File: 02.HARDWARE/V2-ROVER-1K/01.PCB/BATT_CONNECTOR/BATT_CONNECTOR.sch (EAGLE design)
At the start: 16 parts, among them K1 FLEX8, Q1 PJA3416AE_R1_00001

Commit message: Release - SETI_PROTO
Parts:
- removed GND, VCC: TPB2,54, testpad:TPB2,54
- renumbered VBUS to GND_IN
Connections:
- net GND_IN: now also GND_IN.TP; no longer GND.TP, H1.1, H2.1
- net VBUS: now also H1.1, H2.1; no longer GND_IN.TP, VCC.TP
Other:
- moved on the sheet: Q1
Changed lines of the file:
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@@
 <drawing>
 <settings>
-<setting alwaysvectorfont="yes"/>
+<setting alwaysvectorfont="no"/>
 <setting verticaltext="up"/>
 </settings>
-<grid distance="0.05" unitdist="inch" unit="inch" style="lines" multiple="1" display="no" altdistance="0.01" altunitdist="inch" altunit="inch"/>
+<grid distance="0.1" unitdist="inch" unit="inch" style="lines" multiple="1" display="no" altdistance="0.01" altunitdist="inch" altunit="inch"/>
 <layers>
 <layer number="1" name="Top" color="4" fill="1" visible="no" active="no"/>
@@
 <part name="VOUT+" library="testpad" library_urn="urn:adsk.eagle:library:385" deviceset="TP" device="B2,54" package3d_urn="urn:adsk.eagle:package:27948/1"/>
 <part name="VOUT-" library="testpad" library_urn="urn:adsk.eagle:library:385" deviceset="TP" device="B2,54" package3d_urn="urn:adsk.eagle:package:27948/1"/>
-<part name="VBUS" library="testpad" library_urn="urn:adsk.eagle:library:385" deviceset="TP" device="B2,54" package3d_urn="urn:adsk.eagle:package:27948/1"/>
-<part name="GND" library="testpad" library_urn="urn:adsk.eagle:library:385" deviceset="TP" device="B2,54" package3d_urn="urn:adsk.eagle:package:27948/1"/>
+<part name="GND_IN" library="testpad" library_urn="urn:adsk.eagle:library:385" deviceset="TP" device="B2,54" package3d_urn="urn:adsk.eagle:package:27948/1"/>
 <part name="K1" library="Flex_3mm" deviceset="FLEX8" device=""/>
 <part name="VOUT+1" library="testpad" library_urn="urn:adsk.eagle:library:385" deviceset="TP" device="B2,54" package3d_urn="urn:adsk.eagle:package:27948/1"/>
@@
 <part name="SWCLK" library="testpad" library_urn="urn:adsk.eagle:library:385" deviceset="TP" device="B2,54" package3d_urn="urn:adsk.eagle:package:27948/1"/>
 <part name="SWDIO" library="testpad" library_urn="urn:adsk.eagle:library:385" deviceset="TP" device="B2,54" package3d_urn="urn:adsk.eagle:package:27948/1"/>
-<part name="VCC" library="testpad" library_urn="urn:adsk.eagle:library:385" deviceset="TP" device="B2,54" package3d_urn="urn:adsk.eagle:package:27948/1"/>
 <part name="!RESET" library="testpad" library_urn="urn:adsk.eagle:library:385" deviceset="TP" device="B2,54" package3d_urn="urn:adsk.eagle:package:27948/1"/>
 <part name="TXO" library="testpad" library_urn="urn:adsk.eagle:library:385" deviceset="TP" device="B2,54" package3d_urn="urn:adsk.eagle:package:27948/1"/>
@@
 <attribute name="TP_SIGNAL_NAME" x="20.32" y="46.99" size="1.778" layer="97" rot="R90"/>
 </instance>
-<instance part="VBUS" gate="G$1" x="19.05" y="40.64" smashed="yes" rot="R90">
+<instance part="GND_IN" gate="G$1" x="19.05" y="40.64" smashed="yes" rot="R90">
 <attribute name="TP_SIGNAL_NAME" x="20.32" y="41.91" size="1.778" layer="97" rot="R90"/>
-</instance>
-<instance part="GND" gate="G$1" x="19.05" y="30.48" smashed="yes" rot="R90">
-<attribute name="TP_SIGNAL_NAME" x="20.32" y="31.75" size="1.778" layer="97" rot="R90"/>
 </instance>
 <instance part="K1" gate="&gt;NAME" x="106.68" y="58.42" smashed="yes">
@@
 <attribute name="TP_SIGNAL_NAME" x="20.32" y="69.85" size="1.778" layer="97" rot="R90"/>
 </instance>
-<instance part="VCC" gate="G$1" x="19.05" y="76.2" smashed="yes" rot="R90">
-<attribute name="TP_SIGNAL_NAME" x="20.32" y="77.47" size="1.778" layer="97" rot="R90"/>
-</instance>
 <instance part="!RESET" gate="G$1" x="19.05" y="80.01" smashed="yes" rot="R90">
 <attribute name="TP_SIGNAL_NAME" x="20.32" y="81.28" size="1.778" layer="97" rot="R90"/>
@@
 <attribute name="TP_SIGNAL_NAME" x="20.32" y="85.09" size="1.778" layer="97" rot="R90"/>
 </instance>
-<instance part="Q1" gate="A" x="55.88" y="40.64" smashed="yes" rot="R270">
-<attribute name="NAME" x="59.182" y="38.735" size="2.54" layer="95" ratio="10" rot="SR0"/>
+<instance part="Q1" gate="A" x="68.58" y="33.02" smashed="yes" rot="R270">
+<attribute name="NAME" x="71.882" y="31.115" size="2.54" layer="95" ratio="10" rot="SR0"/>
 </instance>
 <instance part="D1" gate="G$1" x="58.42" y="60.96" smashed="yes" rot="R270">
-<attribute name="NAME" x="67.31" y="50.8" size="1.778" layer="95" rot="R270"/>
-<attribute name="VALUE" x="64.77" y="50.8" size="1.778" layer="96" rot="R270"/>
+<attribute name="NAME" x="63.5" y="57.15" size="1.778" layer="95"/>
+<attribute name="VALUE" x="63.5" y="54.61" size="1.778" layer="96"/>
 </instance>
 </instances>
@@
 </segment>
 <segment>
-<pinref part="VCC" gate="G$1" pin="TP"/>
-<wire x1="21.59" y1="76.2" x2="40.64" y2="76.2" width="0.1524" layer="91"/>
-<label x="26.67" y="76.2" size="1.778" layer="95"/>
-</segment>
-<segment>
-<pinref part="VBUS" gate="G$1" pin="TP"/>
-<wire x1="21.59" y1="40.64" x2="40.64" y2="40.64" width="0.1524" layer="91"/>
-<label x="24.13" y="40.64" size="1.778" layer="95"/>
 <pinref part="Q1" gate="A" pin="G"/>
-<wire x1="40.64" y1="40.64" x2="41.91" y2="40.64" width="0.1524" layer="91"/>
-<wire x1="55.88" y1="40.64" x2="41.91" y2="40.64" width="0.1524" layer="91"/>
-</segment>
-</net>
-<net name="SWCLK" class="0">
-<segment>
-<wire x1="104.14" y1="68.58" x2="91.44" y2="68.58" width="0.1524" layer="91"/>
-<pinref part="K1" gate="&gt;NAME" pin="P$5"/>
-<label x="93.98" y="68.58" size="1.778" layer="95"/>
-</segment>
-<segment>
-<pinref part="SWCLK" gate="G$1" pin="TP"/>
-<wire x1="21.59" y1="64.77" x2="39.37" y2="64.77" width="0.1524" layer="91"/>
-<label x="26.67" y="64.77" size="1.778" layer="95"/>
-</segment>
-</net>
-<net name="SWDIO" class="0">
-<segment>
-<label x="93.98" y="76.2" size="1.778" layer="95"/>
-<wire x1="104.14" y1="76.2" x2="91.44" y2="76.2" width="0.1524" layer="91"/>
-<pinref part="K1" gate="&gt;NAME" pin="P$2"/>
-</segment>
-<segment>
-<pinref part="SWDIO" gate="G$1" pin="TP"/>
-<wire x1="21.59" y1="68.58" x2="39.37" y2="68.58" width="0.1524" layer="91"/>
-<label x="26.67" y="68.58" size="1.778" layer="95"/>
-</segment>
-</net>
-<net name="TXO" class="0">
-<segment>
-<label x="93.98" y="71.12" size="1.778" layer="95"/>
-<wire x1="104.14" y1="71.12" x2="91.44" y2="71.12" width="0.1524" layer="91"/>
-<pinref part="K1" gate="&gt;NAME" pin="P$4"/>
-</segment>
-<segment>
-<pinref part="TXO" gate="G$1" pin="TP"/>
-<wire x1="21.59" y1="83.82" x2="40.64" y2="83.82" width="0.1524" layer="91"/>
-<label x="26.67" y="83.82" size="1.778" layer="95"/>
-</segment>
-</net>
-<net name="!RESET" class="0">
-<segment>
-<pinref part="K1" gate="&gt;NAME" pin="P$3"/>
-<wire x1="91.44" y1="73.66" x2="104.14" y2="73.66" width="0.1524" layer="91"/>
-<label x="93.98" y="73.66" size="1.778" layer="95"/>
-</segment>
-<segment>
-<pinref part="!RESET" gate="G$1" pin="TP"/>
-<wire x1="21.59" y1="80.01" x2="40.64" y2="80.01" width="0.1524" layer="91"/>
-<label x="26.67" y="80.01" size="1.778" layer="95"/>
-</segment>
-</net>
-<net name="GND_IN" class="0">
-<segment>
-<pinref part="GND" gate="G$1" pin="TP"/>
+<wire x1="68.58" y1="33.02" x2="53.34" y2="33.02" width="0.1524" layer="91"/>
+<label x="53.34" y="33.02" size="1.778" layer="95" rot="R180" xref="yes"/>
+</segment>
+<segment>
 <pinref part="H2" gate="G$1" pin="1"/>
 <wire x1="21.59" y1="30.48" x2="27.94" y2="30.48" width="0.1524" layer="91"/>
@@
 <wire x1="27.94" y1="30.48" x2="34.29" y2="30.48" width="0.1524" layer="91"/>
 <junction x="27.94" y="30.48"/>
+<label x="25.4" y="30.48" size="1.778" layer="95"/>
+<label x="22.86" y="30.48" size="1.778" layer="95" rot="R180" xref="yes"/>
+</segment>
+</net>
+<net name="SWCLK" class="0">
+<segment>
+<wire x1="104.14" y1="68.58" x2="91.44" y2="68.58" width="0.1524" layer="91"/>
+<pinref part="K1" gate="&gt;NAME" pin="P$5"/>
+<label x="93.98" y="68.58" size="1.778" layer="95"/>
+</segment>
+<segment>
+<pinref part="SWCLK" gate="G$1" pin="TP"/>
+<wire x1="21.59" y1="64.77" x2="39.37" y2="64.77" width="0.1524" layer="91"/>
+<label x="26.67" y="64.77" size="1.778" layer="95"/>
+</segment>
+</net>
+<net name="SWDIO" class="0">
+<segment>
+<label x="93.98" y="76.2" size="1.778" layer="95"/>
+<wire x1="104.14" y1="76.2" x2="91.44" y2="76.2" width="0.1524" layer="91"/>
+<pinref part="K1" gate="&gt;NAME" pin="P$2"/>
+</segment>
+<segment>
+<pinref part="SWDIO" gate="G$1" pin="TP"/>
+<wire x1="21.59" y1="68.58" x2="39.37" y2="68.58" width="0.1524" layer="91"/>
+<label x="26.67" y="68.58" size="1.778" layer="95"/>
+</segment>
+</net>
+<net name="TXO" class="0">
+<segment>
+<label x="93.98" y="71.12" size="1.778" layer="95"/>
+<wire x1="104.14" y1="71.12" x2="91.44" y2="71.12" width="0.1524" layer="91"/>
+<pinref part="K1" gate="&gt;NAME" pin="P$4"/>
+</segment>
+<segment>
+<pinref part="TXO" gate="G$1" pin="TP"/>
+<wire x1="21.59" y1="83.82" x2="40.64" y2="83.82" width="0.1524" layer="91"/>
+<label x="26.67" y="83.82" size="1.778" layer="95"/>
+</segment>
+</net>
+<net name="!RESET" class="0">
+<segment>
+<pinref part="K1" gate="&gt;NAME" pin="P$3"/>
+<wire x1="91.44" y1="73.66" x2="104.14" y2="73.66" width="0.1524" layer="91"/>
+<label x="93.98" y="73.66" size="1.778" layer="95"/>
+</segment>
+<segment>
+<pinref part="!RESET" gate="G$1" pin="TP"/>
+<wire x1="21.59" y1="80.01" x2="40.64" y2="80.01" width="0.1524" layer="91"/>
+<label x="26.67" y="80.01" size="1.778" layer="95"/>
+</segment>
+</net>
+<net name="GND_IN" class="0">
+<segment>
+<pinref part="GND_IN" gate="G$1" pin="TP"/>
+<wire x1="21.59" y1="40.64" x2="33.02" y2="40.64" width="0.1524" layer="91"/>
+<label x="22.86" y="40.64" size="1.778" layer="95"/>
+</segment>
+<segment>
 <pinref part="Q1" gate="A" pin="S"/>
-<wire x1="34.29" y1="30.48" x2="48.26" y2="30.48" width="0.1524" layer="91"/>
-<junction x="34.29" y="30.48"/>
+<wire x1="53.34" y1="22.86" x2="60.96" y2="22.86" width="0.1524" layer="91"/>
+<label x="50.8" y="22.86" size="1.778" layer="95"/>
 </segment>
 </net>
@@
 <segment>
 <pinref part="Q1" gate="A" pin="D"/>
-<wire x1="63.5" y1="30.48" x2="73.66" y2="30.48" width="0.1524" layer="91"/>
-<label x="66.04" y="30.48" size="1.778" layer="95"/>
-</segment>
-<segment>
+<wire x1="76.2" y1="22.86" x2="86.36" y2="22.86" width="0.1524" layer="91"/>
+<label x="78.74" y="22.86" size="1.778" layer="95"/>
+</segment>
+<segment>

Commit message: Cambios Connector Javi Version Final. Pendiente de Revision
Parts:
- added RXI: TPB2,54, testpad:TPB2,54
- K1: value FLEX8 -> FLEX11; device Flex_3mm:FLEX8 -> Flex_3mm:FLEX11
- Q1: value PJA3416AE_R1_00001 -> SSM3J338R,LF; device PJA3416AE_R1_00001:PJA3416AE_R1_00001 -> SSM3J338R_LF:SSM3J338R,LF
- renumbered GND_IN to GND
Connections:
- removed net GND_IN: GND.TP, Q1.S
- new net RXI: K1.P$8, RXI.TP
- new net VBUS_IN: H1.1, H2.1, Q1.D
- net !RESET: now also K1.P$9; no longer K1.P$3
- net GND: now also GND.TP, K1.P$3, K1.P$4, Q1.G; no longer K1.P$8, Q1.D
- net SWCLK: now also K1.P$7; no longer K1.P$5
- net SWDIO: now also K1.P$5; no longer K1.P$2
- net TXO: now also K1.P$6; no longer K1.P$4
- net VBUS: now also K1.P$2, Q1.S; no longer H1.1, H2.1, Q1.G
- net VOUT+: now also K1.P$11; no longer K1.P$7
- net VOUT-: now also K1.P$10; no longer K1.P$6

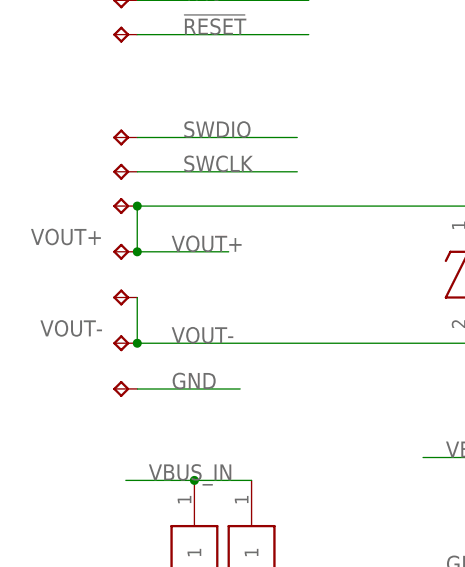
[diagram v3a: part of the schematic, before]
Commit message: Revision para produccion SETI
Faltaba el taladro para GND
Se mueven los testpads para rutado
Se hacen pistas mas gruesas
Se añaden mas vias para facilitar circulacion corriente
Se añaden y depuran las serigrafias
Se genera GERBER
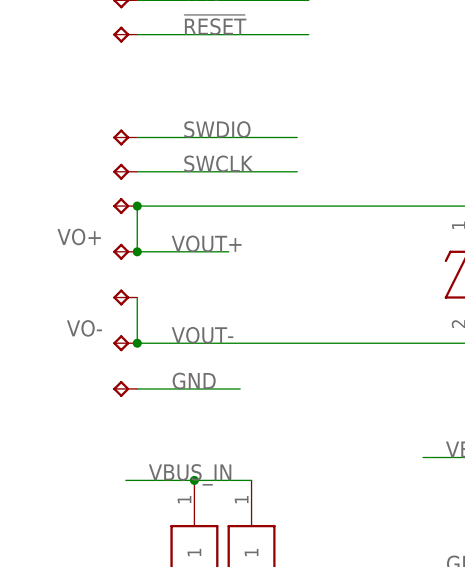
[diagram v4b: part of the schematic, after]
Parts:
- renumbered VOUT+ to VO+, VOUT- to VO-
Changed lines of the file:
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@@
 <drawing>
 <settings>
-<setting alwaysvectorfont="yes"/>
+<setting alwaysvectorfont="no"/>
 <setting verticaltext="up"/>
 </settings>
@@
 </classes>
 <parts>
-<part name="VOUT+" library="testpad" library_urn="urn:adsk.eagle:library:385" deviceset="TP" device="B2,54" package3d_urn="urn:adsk.eagle:package:27948/1"/>
-<part name="VOUT-" library="testpad" library_urn="urn:adsk.eagle:library:385" deviceset="TP" device="B2,54" package3d_urn="urn:adsk.eagle:package:27948/1"/>
+<part name="VO+" library="testpad" library_urn="urn:adsk.eagle:library:385" deviceset="TP" device="B2,54" package3d_urn="urn:adsk.eagle:package:27948/1"/>
+<part name="VO-" library="testpad" library_urn="urn:adsk.eagle:library:385" deviceset="TP" device="B2,54" package3d_urn="urn:adsk.eagle:package:27948/1"/>
 <part name="GND" library="testpad" library_urn="urn:adsk.eagle:library:385" deviceset="TP" device="B2,54" package3d_urn="urn:adsk.eagle:package:27948/1"/>
 <part name="K1" library="Flex_3mm" deviceset="FLEX11" device=""/>
@@
 </plain>
 <instances>
-<instance part="VOUT+" gate="G$1" x="19.05" y="55.88" smashed="yes" rot="R90">
+<instance part="VO+" gate="G$1" x="19.05" y="55.88" smashed="yes" rot="R90">
 <attribute name="NAME" x="17.78" y="58.42" size="1.778" layer="95" rot="R180"/>
 <attribute name="TP_SIGNAL_NAME" x="20.32" y="57.15" size="1.778" layer="97" rot="R90"/>
 </instance>
-<instance part="VOUT-" gate="G$1" x="19.05" y="45.72" smashed="yes" rot="R90">
+<instance part="VO-" gate="G$1" x="19.05" y="45.72" smashed="yes" rot="R90">
 <attribute name="NAME" x="17.78" y="48.26" size="1.778" layer="95" rot="R180"/>
 <attribute name="TP_SIGNAL_NAME" x="20.32" y="46.99" size="1.778" layer="97" rot="R90"/>
@@
 <segment>
 <pinref part="VOUT+1" gate="G$1" pin="TP"/>
-<pinref part="VOUT+" gate="G$1" pin="TP"/>
+<pinref part="VO+" gate="G$1" pin="TP"/>
 <wire x1="21.59" y1="60.96" x2="21.59" y2="55.88" width="0.1524" layer="91"/>
 <wire x1="21.59" y1="55.88" x2="31.75" y2="55.88" width="0.1524" layer="91"/>
@@
 <segment>
 <pinref part="VOUT-1" gate="G$1" pin="TP"/>
-<pinref part="VOUT-" gate="G$1" pin="TP"/>
+<pinref part="VO-" gate="G$1" pin="TP"/>
 <wire x1="21.59" y1="50.8" x2="21.59" y2="45.72" width="0.1524" layer="91"/>
 <junction x="21.59" y="45.72"/>

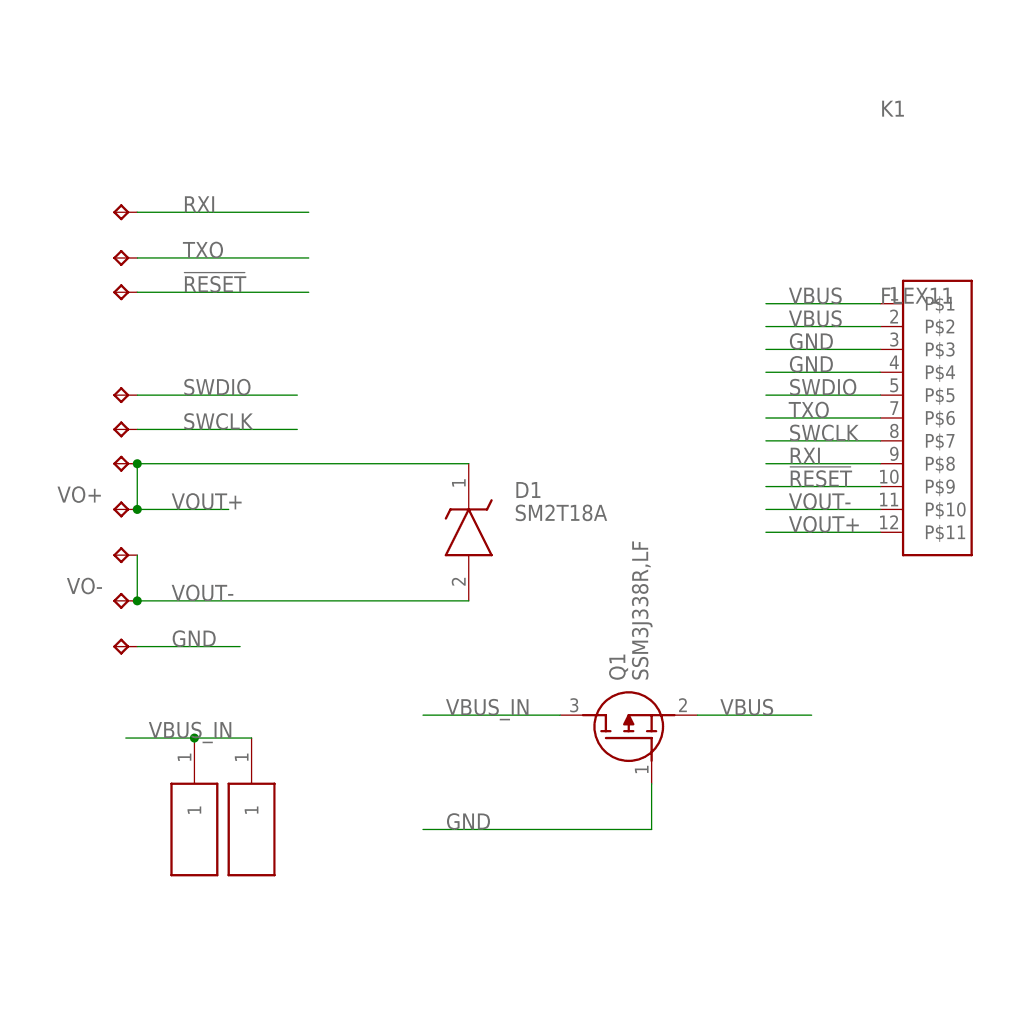
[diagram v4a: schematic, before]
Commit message: BOM PCB Connector Actualizada y SCH
Se actualiza la BOM con el nuevo transistor Q1 DMG3415U-7
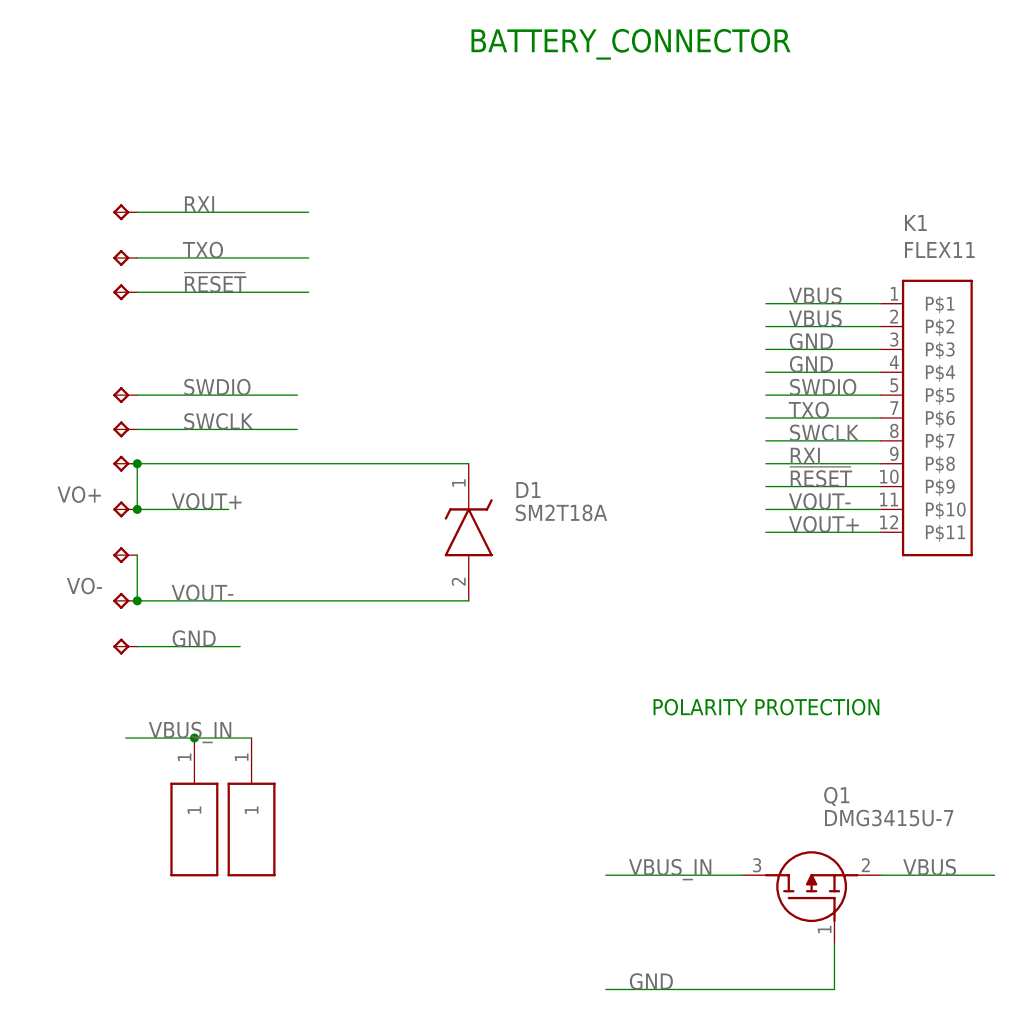
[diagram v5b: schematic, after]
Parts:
- Q1: value SSM3J338R,LF -> DMG3415U-7
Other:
- note added: "BATTERY_CONNECTOR"
- note added: "POLARITY PROTECTION"
- moved on the sheet: Q1
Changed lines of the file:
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@@
 <part name="D1" library="SM2T18A" deviceset="SM2T18A" device=""/>
 <part name="RXI" library="testpad" library_urn="urn:adsk.eagle:library:385" deviceset="TP" device="B2,54" package3d_urn="urn:adsk.eagle:package:27948/1"/>
-<part name="Q1" library="SSM3J338R_LF" deviceset="SSM3J338R,LF" device=""/>
+<part name="Q1" library="SSM3J338R_LF" deviceset="SSM3J338R,LF" device="" value="DMG3415U-7"/>
 </parts>
 <sheets>
 <sheet>
 <plain>
+<text x="78.74" y="33.02" size="1.778" layer="91">POLARITY PROTECTION</text>
+<text x="58.42" y="106.68" size="2.54" layer="91">BATTERY_CONNECTOR</text>
 </plain>
 <instances>
@@
 </instance>
 <instance part="K1" gate="G$1" x="106.68" y="81.28" smashed="yes">
-<attribute name="NAME" x="104.14" y="99.52" size="1.778" layer="95"/>
-<attribute name="VALUE" x="104.14" y="78.74" size="1.778" layer="96"/>
+<attribute name="NAME" x="106.68" y="86.82" size="1.778" layer="95"/>
+<attribute name="VALUE" x="106.68" y="83.82" size="1.778" layer="96"/>
 </instance>
 <instance part="VOUT+1" gate="G$1" x="19.05" y="60.96" smashed="yes" rot="R90">
@@
 <attribute name="TP_SIGNAL_NAME" x="20.32" y="90.17" size="1.778" layer="97" rot="R90"/>
 </instance>
-<instance part="Q1" gate="G$1" x="78.74" y="25.4" smashed="yes" rot="R90">
-<attribute name="NAME" x="74.93" y="36.83" size="1.778" layer="95" rot="R90" align="center-left"/>
-<attribute name="VALUE" x="77.47" y="36.83" size="1.778" layer="96" rot="R90" align="center-left"/>
+<instance part="Q1" gate="G$1" x="99.06" y="7.62" smashed="yes" rot="R90">
+<attribute name="NAME" x="97.79" y="24.13" size="1.778" layer="95" align="center-left"/>
+<attribute name="VALUE" x="97.79" y="21.59" size="1.778" layer="96" align="center-left"/>
 </instance>
 </instances>
@@
 <segment>
 <pinref part="Q1" gate="G$1" pin="S"/>
-<wire x1="83.82" y1="33.02" x2="96.52" y2="33.02" width="0.1524" layer="91"/>
-<label x="86.36" y="33.02" size="1.778" layer="95"/>
+<wire x1="104.14" y1="15.24" x2="116.84" y2="15.24" width="0.1524" layer="91"/>
+<label x="106.68" y="15.24" size="1.778" layer="95"/>
 </segment>
 </net>
@@
 <segment>
 <pinref part="Q1" gate="G$1" pin="G"/>
-<wire x1="78.74" y1="25.4" x2="78.74" y2="20.32" width="0.1524" layer="91"/>
-<wire x1="78.74" y1="20.32" x2="53.34" y2="20.32" width="0.1524" layer="91"/>
-<label x="55.88" y="20.32" size="1.778" layer="95"/>
+<wire x1="99.06" y1="7.62" x2="99.06" y2="2.54" width="0.1524" layer="91"/>
+<wire x1="99.06" y1="2.54" x2="73.66" y2="2.54" width="0.1524" layer="91"/>
+<label x="76.2" y="2.54" size="1.778" layer="95"/>
 </segment>
 </net>
@@
 <segment>
 <pinref part="Q1" gate="G$1" pin="D"/>
-<wire x1="68.58" y1="33.02" x2="53.34" y2="33.02" width="0.1524" layer="91"/>
-<label x="55.88" y="33.02" size="1.778" layer="95"/>
-</segment>
-<segment>
+<wire x1="88.9" y1="15.24" x2="73.66" y2="15.24" width="0.1524" layer="91"/>
+<label x="76.2" y="15.24" size="1.778" layer="95"/>
+</segment>
+<segment>
